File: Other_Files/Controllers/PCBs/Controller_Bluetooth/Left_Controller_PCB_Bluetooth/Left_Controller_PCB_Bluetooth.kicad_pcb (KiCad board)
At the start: 2 copper layers, 53 x 102 mm, 13 parts

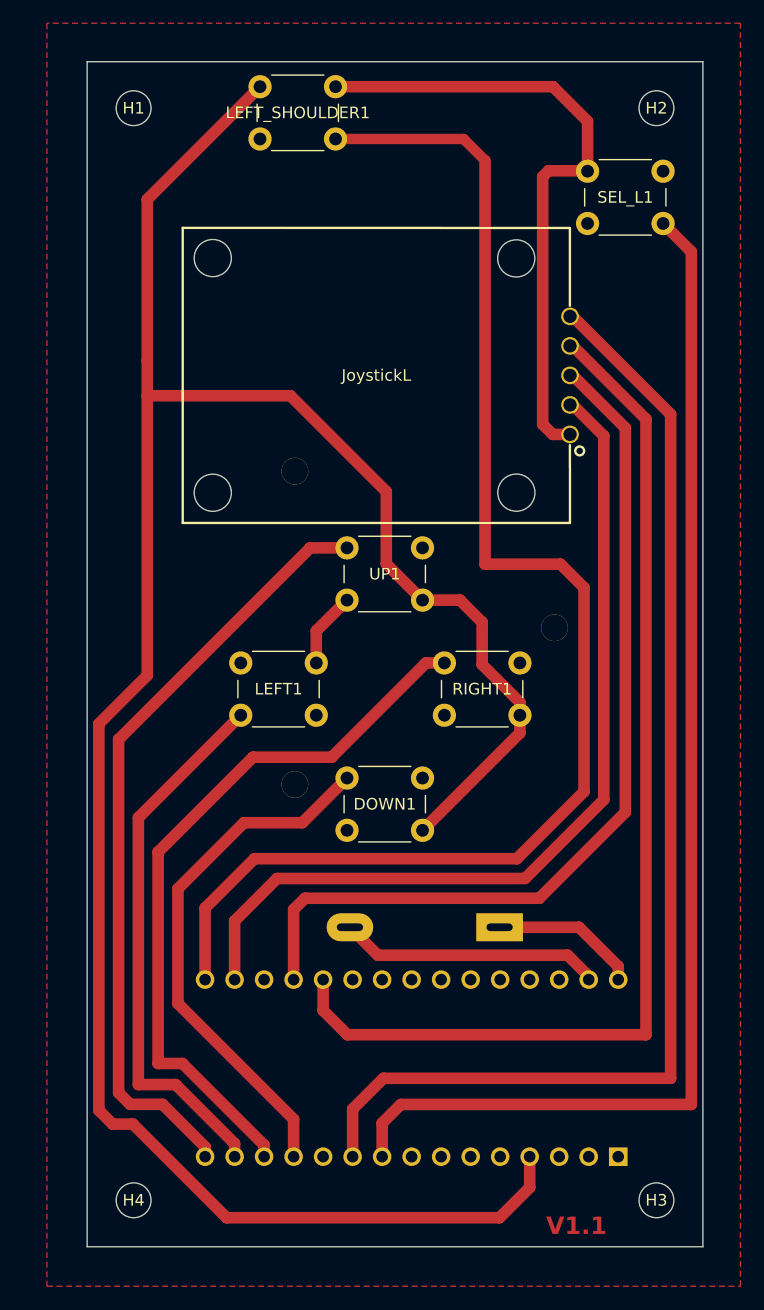
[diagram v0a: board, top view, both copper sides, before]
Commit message: Updated the Controllers' PCB to version 1.2
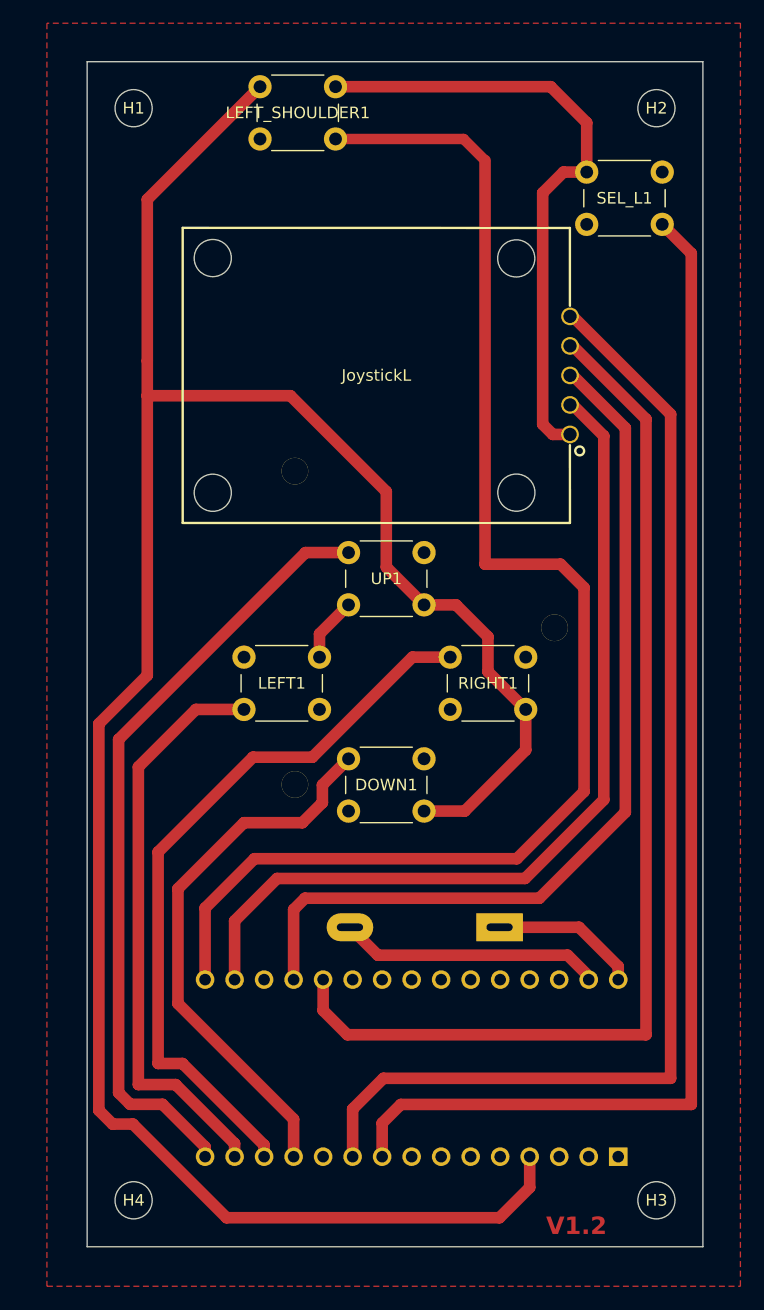
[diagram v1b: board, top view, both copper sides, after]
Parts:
- H1, H2, H3, H4: footprint MountingHole:MountingHole_3mm -> MountingHole:MountingHole_3.2mm_M3
- moved DOWN1 1.66 mm to (139.5, 107.0)
- moved RIGHT1 0.71 mm to (148.2, 98.2)
- moved LEFT1 0.57 mm to (130.5, 98.2)
- moved UP1 0.43 mm to (139.5, 89.2)
- moved SEL_L1 0.10 mm to (166.5, 61.0)
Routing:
- net /LEFT: track 47.0 -> 50.0 mm
- net /DOWN: track 45.7 -> 47.4 mm
- net GND: track 286.2 -> 284.7 mm
- net /RIGHT: track 62.6 -> 63.3 mm
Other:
- board text added: "V1.2"
- board text removed: "V1.1"

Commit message: Updated Bluetooth Controllers' PCBs
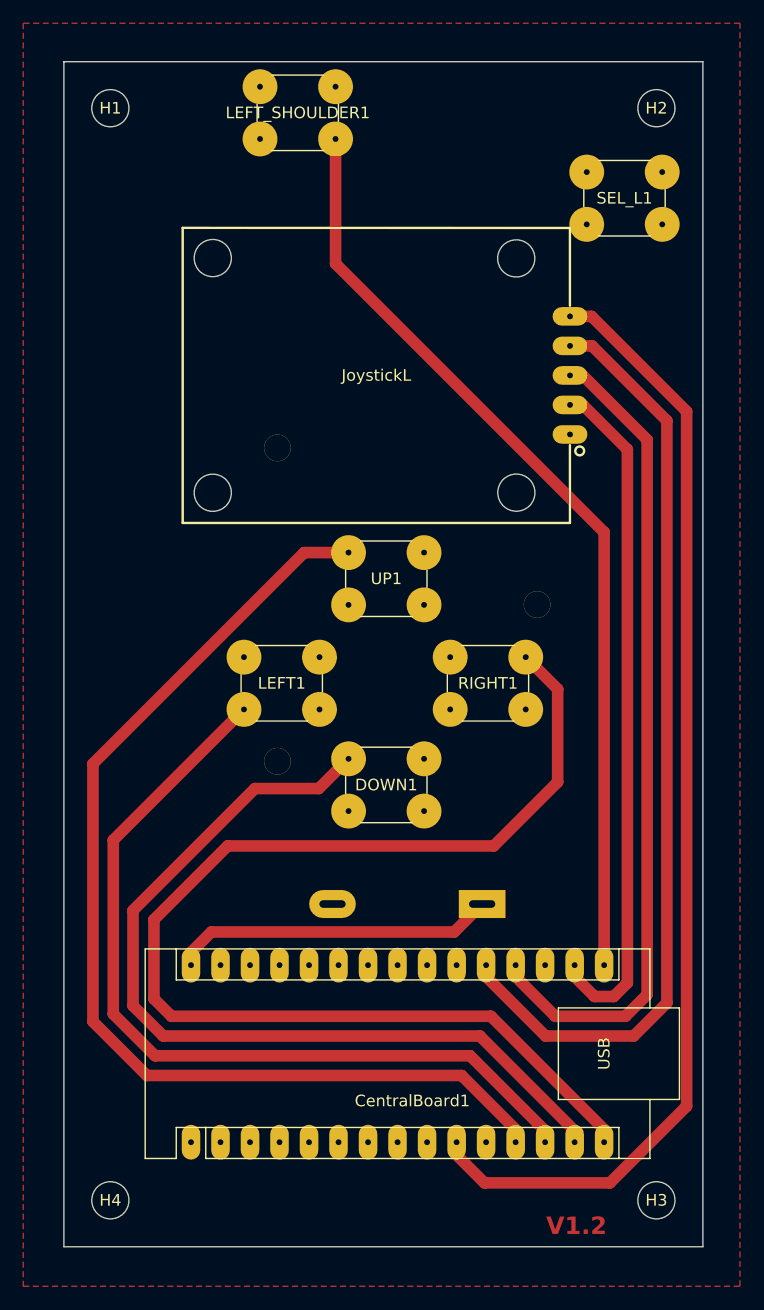
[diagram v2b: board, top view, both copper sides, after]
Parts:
- CentralBoard1: moved to F.Cu
- moved CentralBoard1 36.8 mm to (125.9, 140.0)
- moved BAT9V1 2.50 mm to (151.0, 119.5)
- moved H1 2.00 mm to (119.0, 51.0)
- moved H4 2.00 mm to (119.0, 145.0)
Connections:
- CentralBoard1 pad 12: /DOWN -> /UP
- CentralBoard1 pad 13: /RIGHT -> /LEFT
- CentralBoard1 pad 14: /LEFT -> /DOWN
- CentralBoard1 pad 15: /UP -> /RIGHT
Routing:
- net GND: track 284.7 -> 0.05 mm
- net /SEL_L: track 106.9 -> 0.00 mm
- net /RIGHT: track 63.3 -> 102.9 mm
- net /LEFT_SHOULDER: track 118.2 -> 80.7 mm
- net /DOWN: track 47.4 -> 75.6 mm
- net /UP: track 67.1 -> 93.0 mm
- net /LEFT: track 50.0 -> 73.2 mm
- net +3.3V: track 76.5 -> 59.2 mm
- net +9V: track 12.7 -> 27.9 mm
- net /Analog_Y_L: track 93.4 -> 81.0 mm
- net /Analog_X_L: track 77.8 -> 71.2 mm
- net /SEL_JOY_L: track 101.9 -> 97.9 mm
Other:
- board size 53 x 102 mm -> 55 x 102 mm
